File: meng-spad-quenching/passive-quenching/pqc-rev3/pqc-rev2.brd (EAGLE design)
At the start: 38.1 x 25.4 mm, 61 parts, among them IC1 OPA858, IC2 OPA858, IC4 TPS7A4901, X1 CONN_SPAD, X2 PWR, X4 VBIAS_IN, X5 SIGNAL_OUT

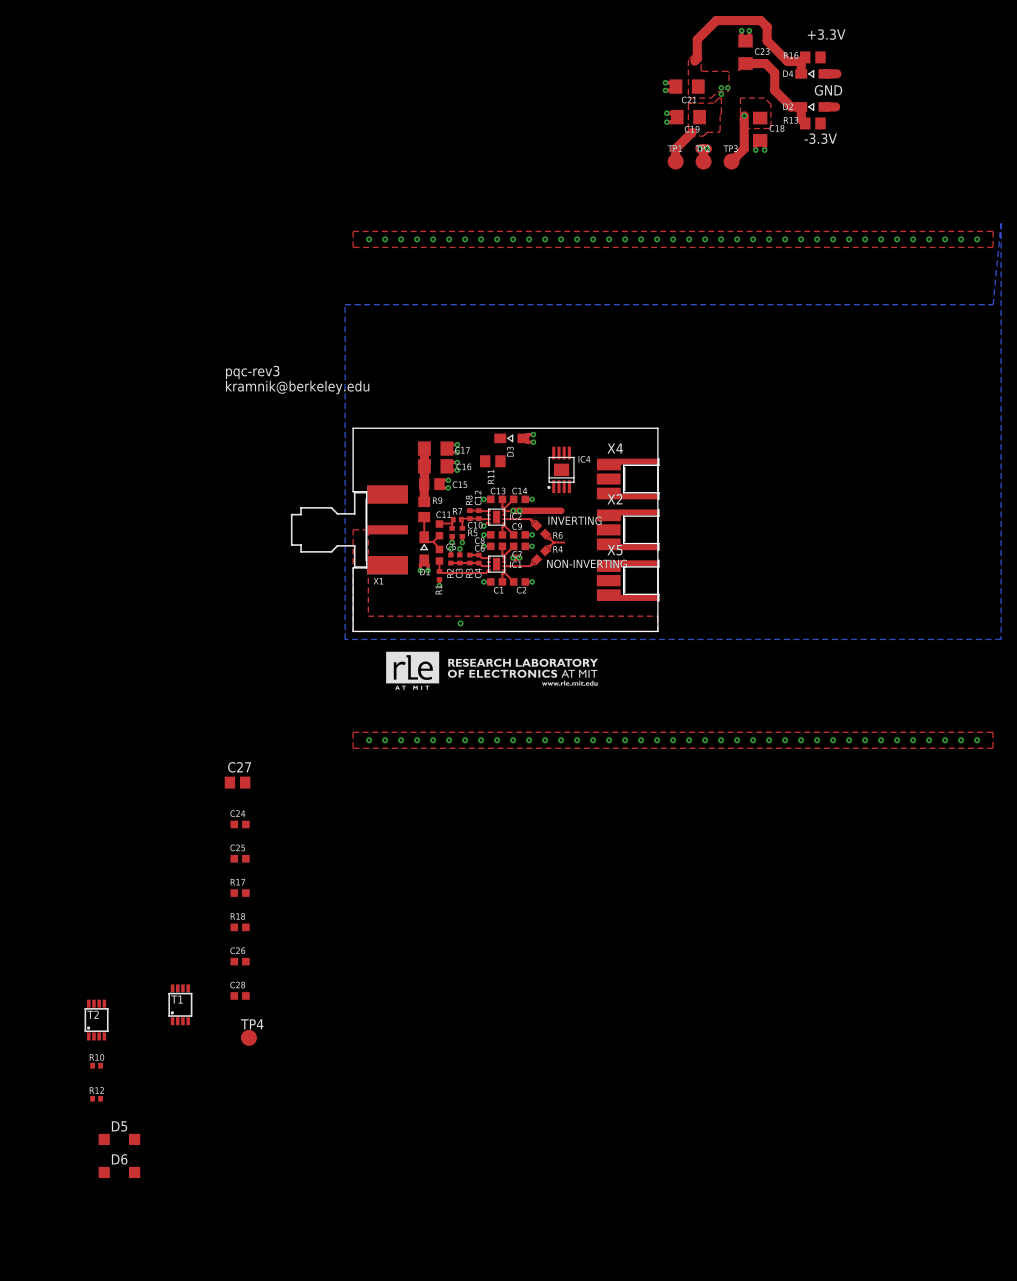
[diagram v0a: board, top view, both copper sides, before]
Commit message: Sim working with stand-ins for NMOS and PMOS switches
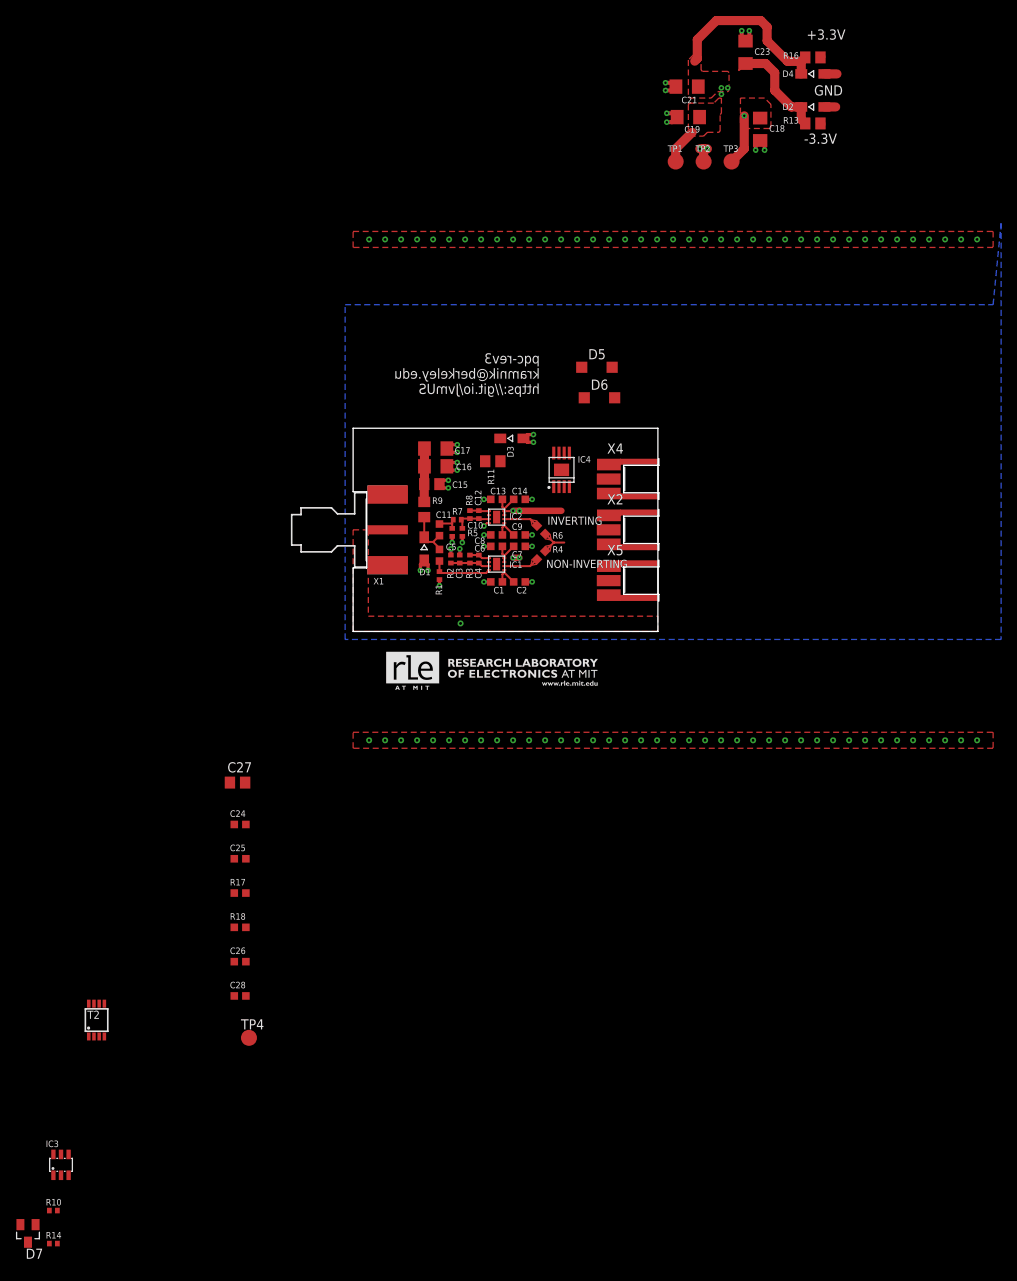
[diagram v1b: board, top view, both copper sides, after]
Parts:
- removed R12: RPU, rcl-modified-footprints:R0402
- removed T1: (no value), zetex:MSOP8
- added D7: BZX84C6V2L, diode:SOT23
- added IC3: NUD3160DMT1G, meng:SOT23-6L
- added R14: RES SMD 33K OHM 1% 1/10W 0603, rcl-modified-footprints:R0402
- R10: value RPD -> RES SMD 33K OHM 1% 1/10W 0603
- X2: value PWR -> VIN_PWR
- X4: value VBIAS_IN -> VIN_BIAS
- moved D6 113.9 mm to (30.8, 29.2)
- moved D5 113.5 mm to (30.5, 33.0)
- moved R10 18.9 mm to (-37.5, -72.4)
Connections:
- removed net N$8: R12.1, T2.4, T2.7, T2.8
- new net LOAD_SW_PMOS_GATE: D7.1, IC3.3, T2.4
- new net LOAD_SW_PMOS_SOURCE: D5.C, D7.3, R10.2, T2.3
- new net N$14: D6.A, IC3.2, X2.1
- new net N$15: IC3.4, R14.2
- net GND: now also IC3.1, R14.1; no longer R10.1, T2.1
- net N$9: now also IC3.5, IC3.6, R10.1; no longer R10.2, T2.2, X2.1
- net PP_P15V0_ANALOG: now also D6.C
- net VBIAS_IN: now also D5.A; no longer R12.2, T2.3
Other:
- board text added: "pqc-rev3 kramnik@berkeley.edu https://git.io/JvmUS"
- board text removed: "pqc-rev3 kramnik@berkeley.edu"
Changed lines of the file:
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@@
 <rectangle x1="4.1259125" y1="-2.5479375" x2="10.7616625" y2="-2.5447625" layer="21"/>
 <rectangle x1="4.1259125" y1="-2.5447625" x2="10.7616625" y2="-2.5415875" layer="21"/>
-<text x="-16.03375" y="30.00375" size="1.27" layer="21" font="vector" ratio="16">pqc-rev3
-kramnik@berkeley.edu</text>
+<text x="23.33625" y="29.68625" size="1.27" layer="21" font="vector" ratio="16" rot="MR0">pqc-rev3
+kramnik@berkeley.edu
+https://git.io/JvmUS</text>
 </plain>
 <attributes>
@@
 <attribute name="NAME" x="12.7" y="22.225" size="0.8128" layer="25" font="vector" ratio="16"/>
 </element>
-<element name="X4" library="con-samtec" library_urn="urn:adsk.eagle:library:184" package="MMCX-J-P-X-ST-EM1-MKT" value="VBIAS_IN" x="38.1" y="19.05" smashed="yes" rot="R270">
+<element name="X4" library="con-samtec" library_urn="urn:adsk.eagle:library:184" package="MMCX-J-P-X-ST-EM1-MKT" value="VIN_BIAS" x="38.1" y="19.05" smashed="yes" rot="R270">
 <attribute name="MF" value="Samtec Inc." x="38.1" y="19.05" size="1.778" layer="27" rot="R270" display="off"/>
 <attribute name="MPN" value="MMCX-J-P-X-ST-EM1-MKT" x="38.1" y="19.05" size="1.778" layer="27" rot="R270" display="off"/>
@@
 <attribute name="VALUE" x="-15.39875" y="-47.14875" size="0.8128" layer="27" font="vector" ratio="16"/>
 </element>
-<element name="X2" library="con-samtec" library_urn="urn:adsk.eagle:library:184" package="MMCX-J-P-X-ST-EM1-MKT" value="PWR" x="38.1" y="12.7" smashed="yes" rot="R270">
+<element name="X2" library="con-samtec" library_urn="urn:adsk.eagle:library:184" package="MMCX-J-P-X-ST-EM1-MKT" value="VIN_PWR" x="38.1" y="12.7" smashed="yes" rot="R270">
 <attribute name="MF" value="Samtec Inc." x="38.1" y="12.7" size="1.778" layer="27" rot="R270" display="off"/>
 <attribute name="MPN" value="MMCX-J-P-X-ST-EM1-MKT" x="38.1" y="12.7" size="1.778" layer="27" rot="R270" display="off"/>
@@
 <attribute name="TP_SIGNAL_NAME" value="" x="-13.0175" y="-53.34" size="1" layer="37"/>
 <attribute name="VALUE" x="-13.7795" y="-51.816" size="0.0254" layer="27"/>
-</element>
-<element name="T1" library="zetex" library_urn="urn:adsk.eagle:library:418" package="MSOP8" package3d_urn="urn:adsk.eagle:package:30988/2" value="" x="-21.59" y="-46.6725" smashed="yes">
-<attribute name="MF" value="" x="-21.59" y="-46.6725" size="1.778" layer="27" display="off"/>
-<attribute name="MPN" value="" x="-21.59" y="-46.6725" size="1.778" layer="27" display="off"/>
-<attribute name="NAME" x="-22.74" y="-46.5225" size="1.016" layer="25"/>
-<attribute name="OC_FARNELL" value="1412091" x="-21.59" y="-46.6725" size="1.778" layer="27" display="off"/>
-<attribute name="OC_NEWARK" value="unknown" x="-21.59" y="-46.6725" size="1.778" layer="27" display="off"/>
-<attribute name="VALUE" x="-22.24" y="-47.7225" size="1.016" layer="27"/>
 </element>
 <element name="T2" library="zetex" library_urn="urn:adsk.eagle:library:418" package="MSOP8" package3d_urn="urn:adsk.eagle:package:30988/2" value="" x="-32.0675" y="-48.5775" smashed="yes">
@@
 <attribute name="VALUE" x="-32.7175" y="-49.6275" size="1.016" layer="27"/>
 </element>
-<element name="R10" library="rcl-modified-footprints" package="R0402" package3d_urn="urn:adsk.eagle:package:23547/1" value="RPD" x="-32.0675" y="-54.2925" smashed="yes">
-<attribute name="NAME" x="-33.02" y="-53.6575" size="0.8128" layer="25" font="vector" ratio="16"/>
-<attribute name="VALUE" x="-33.02" y="-55.88" size="0.8128" layer="27" font="vector" ratio="16"/>
-</element>
-<element name="R12" library="rcl-modified-footprints" package="R0402" package3d_urn="urn:adsk.eagle:package:23547/1" value="RPU" x="-32.0675" y="-58.42" smashed="yes">
-<attribute name="NAME" x="-33.02" y="-57.785" size="0.8128" layer="25" font="vector" ratio="16"/>
-<attribute name="VALUE" x="-33.02" y="-60.0075" size="0.8128" layer="27" font="vector" ratio="16"/>
-</element>
-<element name="D5" library="diode" library_urn="urn:adsk.eagle:library:210" package="SOD123" package3d_urn="urn:adsk.eagle:package:43420/1" value="MMSD4148" x="-29.21" y="-63.5"/>
-<element name="D6" library="diode" library_urn="urn:adsk.eagle:library:210" package="SOD123" package3d_urn="urn:adsk.eagle:package:43420/1" value="MMSD4148" x="-29.21" y="-67.6275"/>
+<element name="D5" library="diode" library_urn="urn:adsk.eagle:library:210" package="SOD123" package3d_urn="urn:adsk.eagle:package:43420/1" value="MMSD4148" x="30.48" y="33.02"/>
+<element name="D6" library="diode" library_urn="urn:adsk.eagle:library:210" package="SOD123" package3d_urn="urn:adsk.eagle:package:43420/1" value="MMSD4148" x="30.7975" y="29.21"/>
+<element name="IC3" library="meng" package="SOT23-6L" value="NUD3160DMT1G" x="-36.5125" y="-66.675"/>
+<element name="R10" library="rcl-modified-footprints" package="R0402" package3d_urn="urn:adsk.eagle:package:23547/1" value="RES SMD 33K OHM 1% 1/10W 0603" x="-37.465" y="-72.39"/>
+<element name="R14" library="rcl-modified-footprints" package="R0402" package3d_urn="urn:adsk.eagle:package:23547/1" value="RES SMD 33K OHM 1% 1/10W 0603" x="-37.465" y="-76.5175"/>
+<element name="D7" library="diode" library_urn="urn:adsk.eagle:library:210" package="SOT23" package3d_urn="urn:adsk.eagle:package:43389/2" value="BZX84C6V2L" x="-40.64" y="-75.2475" rot="R180"/>
 </elements>
 <signals>
@@
 <contactref element="X2" pad="2@4"/>
 <contactref element="X2" pad="2@1"/>
-<contactref element="T2" pad="1"/>
-<contactref element="R10" pad="1"/>
+<contactref element="IC3" pad="1"/>
+<contactref element="R14" pad="1"/>
 <wire x1="58.9175" y1="65.56375" x2="58.9175" y2="69.69125" width="0" layer="19" extent="1-1"/>
 <wire x1="51.435" y1="61.135" x2="58.9175" y2="65.56375" width="0" layer="19" extent="1-1"/>
@@
 <wire x1="-13.40375" y1="-41.275" x2="-13.40375" y2="-36.98875" width="0" layer="19" extent="1-1"/>
 <wire x1="-13.40375" y1="-45.56125" x2="-13.40375" y2="-41.275" width="0" layer="19" extent="1-1"/>
-<wire x1="-33.0425" y1="-50.6275" x2="-13.40375" y2="-45.56125" width="0" layer="19" extent="1-1"/>
-<wire x1="-32.5675" y1="-54.2925" x2="-33.0425" y2="-50.6275" width="0" layer="19" extent="1-1"/>
+<wire x1="-37.4625" y1="-67.975" x2="-13.40375" y2="-45.56125" width="0" layer="19" extent="1-1"/>
+<wire x1="-37.965" y1="-76.5175" x2="-37.4625" y2="-67.975" width="0" layer="19" extent="1-1"/>
 </signal>
 <signal name="PP_PVIN">
@@
 <contactref element="R11" pad="2"/>
 <contactref element="X4" pad="1"/>
-<contactref element="T2" pad="3"/>
-<contactref element="R12" pad="2"/>
-<wire x1="-31.7425" y1="-50.6275" x2="-31.5675" y2="-58.42" width="0" layer="19" extent="1-1"/>
-<wire x1="18.4125" y1="21.2725" x2="-31.7425" y2="-50.6275" width="0" layer="19" extent="1-1"/>
+<contactref element="D5" pad="A"/>
+<wire x1="18.4125" y1="21.2725" x2="32.38" y2="33.02" width="0" layer="19" extent="1-1"/>
 <wire x1="18.39375" y1="24.13" x2="18.4125" y2="21.2725" width="0" layer="19" extent="1-1"/>
 <wire x1="31.95" y1="19.05" x2="18.4125" y2="21.2725" width="0" layer="19" extent="1-1"/>
@@
 <contactref element="T2" pad="5"/>
 <contactref element="T2" pad="6"/>
+<contactref element="D6" pad="C"/>
+<wire x1="-31.0925" y1="-46.5275" x2="28.8975" y2="29.21" width="0" layer="19" extent="1-1"/>
 <wire x1="-31.7425" y1="-46.5275" x2="-31.0925" y2="-46.5275" width="0" layer="19" extent="1-1"/>
 <wire x1="-14.85375" y1="-45.56125" x2="-31.0925" y2="-46.5275" width="0" layer="19" extent="1-1"/>
@@
 <wire x1="25.7325" y1="18.0975" x2="-13.40375" y2="-28.41625" width="0" layer="19" extent="1-1"/>
 </signal>
-<signal name="N$8">
-<contactref element="R12" pad="1"/>
+<signal name="LOAD_SW_PMOS_GATE">
 <contactref element="T2" pad="4"/>
-<contactref element="T2" pad="8" route="any" routetag="1.D"/>
-<contactref element="T2" pad="7" route="any" routetag="1.D"/>
-<wire x1="-31.0925" y1="-50.6275" x2="-32.5675" y2="-58.42" width="0" layer="19" extent="1-1"/>
-<wire x1="-32.3925" y1="-46.5275" x2="-31.0925" y2="-50.6275" width="0" layer="19" extent="1-1"/>
+<contactref element="IC3" pad="3"/>
+<contactref element="D7" pad="1"/>
+<wire x1="-35.5625" y1="-67.975" x2="-39.69" y2="-74.1475" width="0" layer="19" extent="1-1"/>
+<wire x1="-31.0925" y1="-50.6275" x2="-35.5625" y2="-67.975" width="0" layer="19" extent="1-1"/>
+</signal>
+<signal name="LOAD_SW_PMOS_SOURCE">
+<contactref element="D5" pad="C"/>
+<contactref element="T2" pad="3"/>
+<contactref element="R10" pad="2"/>
+<contactref element="D7" pad="3"/>
+<wire x1="-36.965" y1="-72.39" x2="-40.64" y2="-76.3475" width="0" layer="19" extent="1-1"/>
+<wire x1="28.58" y1="33.02" x2="-36.965" y2="-72.39" width="0" layer="19" extent="1-1"/>
+<wire x1="-31.7425" y1="-50.6275" x2="28.58" y2="33.02" width="0" layer="19" extent="1-1"/>
 </signal>
 <signal name="N$9">
-<contactref element="R10" pad="2"/>
-<contactref element="T2" pad="2"/>
+<contactref element="IC3" pad="6"/>
+<contactref element="IC3" pad="5"/>
+<contactref element="R10" pad="1"/>
+<wire x1="-37.4625" y1="-65.375" x2="-37.965" y2="-72.39" width="0" layer="19" extent="1-1"/>
+<wire x1="-36.5125" y1="-65.375" x2="-37.4625" y2="-65.375" width="0" layer="19" extent="1-1"/>
+</signal>
+<signal name="N$14">
 <contactref element="X2" pad="1"/>
-<wire x1="-32.3925" y1="-50.6275" x2="-31.5675" y2="-54.2925" width="0" layer="19" extent="1-1"/>
-<wire x1="31.95" y1="12.7" x2="-32.3925" y2="-50.6275" width="0" layer="19" extent="1-1"/>
+<contactref element="IC3" pad="2"/>
+<contactref element="D6" pad="A"/>
+<wire x1="32.6975" y1="29.21" x2="-36.5125" y2="-67.975" width="0" layer="19" extent="1-1"/>
+<wire x1="31.95" y1="12.7" x2="32.6975" y2="29.21" width="0" layer="19" extent="1-1"/>
+</signal>
+<signal name="N$15">
+<contactref element="IC3" pad="4"/>
+<contactref element="R14" pad="2"/>
+<wire x1="-35.5625" y1="-65.375" x2="-36.965" y2="-76.5175" width="0" layer="19" extent="1-1"/>
 </signal>
 </signals>
